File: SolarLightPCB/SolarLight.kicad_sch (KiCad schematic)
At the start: 15 parts, among them J1 I2C, J2 SPI, SW1 Switch, SW2 ON_OFF, U1 TP4056, U2 WeMos_D1_mini

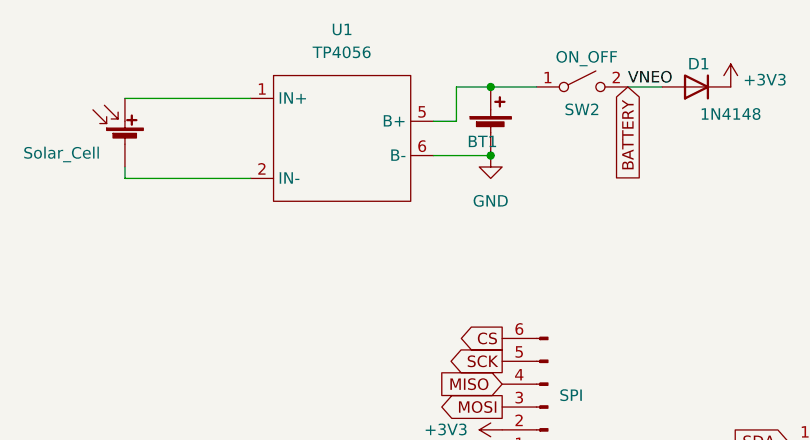
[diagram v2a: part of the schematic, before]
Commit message: Update TP4056 library
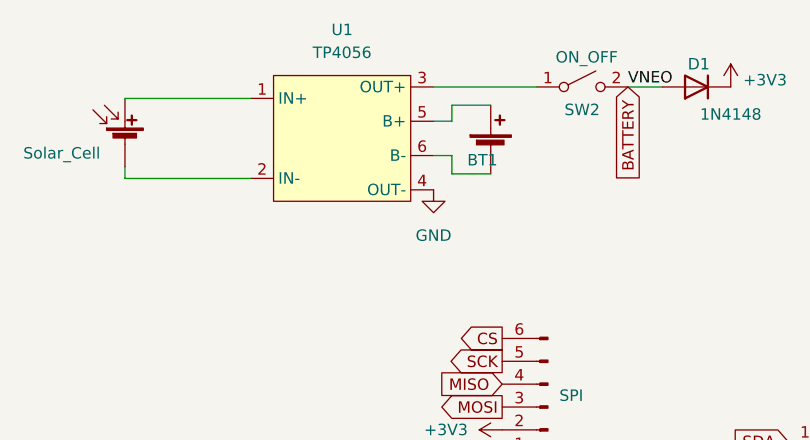
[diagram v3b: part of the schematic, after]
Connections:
- net GND: now also U1.4 (OUT-); no longer BT1.2 (-), U1.6 (B-)
- net at BT1.1 (+), U1.5 (B+): no longer SW2.1 (A)
- new net: BT1.2 (-), U1.6 (B-)
- new net: SW2.1 (A), U1.3 (OUT+)
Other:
- moved on the sheet: BT1
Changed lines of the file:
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@@
     (company "Fablab Zürich / Beat Besmer / Bernd Heistercamp")
   )
-  (junction (at 157.48 38.1) (diameter 0) (color 0 0 0 0)
-  )
   (junction (at 217.932 105.918) (diameter 0) (color 0 0 0 0)
   )
   (junction (at 214.63 97.028) (diameter 0) (color 0 0 0 0)
-  )
-  (junction (at 157.48 45.72) (diameter 0) (color 0 0 0 0)
   )
   (no_connect (at 109.728 103.124))
@@
   (no_connect (at 146.05 114.3))
   (no_connect (at 146.05 116.84))
+  (wire (pts (xy 157.48 40.132) (xy 153.162 40.132))
+    (stroke (width 0) (type default) (color 0 0 0 0))
+  )
+  (wire (pts (xy 153.162 47.752) (xy 157.48 47.752))
+    (stroke (width 0) (type default) (color 0 0 0 0))
+  )
   (wire (pts (xy 214.63 97.028) (xy 221.742 97.028))
     (stroke (width 0) (type default) (color 0 0 0 0))
@@
     (stroke (width 0) (type default) (color 0 0 0 0))
   )
+  (wire (pts (xy 153.162 41.91) (xy 151.13 41.91))
+    (stroke (width 0) (type default) (color 0 0 0 0))
+  )
+  (wire (pts (xy 151.13 45.72) (xy 153.162 45.72))
+    (stroke (width 0) (type default) (color 0 0 0 0))
+  )
   (wire (pts (xy 116.84 48.26) (xy 116.84 46.99))
     (stroke (width 0) (type default) (color 0 0 0 0))
@@
     (stroke (width 0) (type default) (color 0 0 0 0))
   )
-  (wire (pts (xy 153.67 38.1) (xy 153.67 41.91))
-    (stroke (width 0) (type default) (color 0 0 0 0))
-  )
   (wire (pts (xy 130.81 48.26) (xy 116.84 48.26))
     (stroke (width 0) (type default) (color 0 0 0 0))
   )
-  (wire (pts (xy 151.13 41.91) (xy 153.67 41.91))
+  (wire (pts (xy 151.13 38.1) (xy 162.56 38.1))
     (stroke (width 0) (type default) (color 0 0 0 0))
   )
@@
     (stroke (width 0) (type default) (color 0 0 0 0))
   )
-  (wire (pts (xy 151.13 45.72) (xy 157.48 45.72))
-    (stroke (width 0) (type default) (color 0 0 0 0))
-  )
-  (wire (pts (xy 157.48 38.1) (xy 153.67 38.1))
+  (wire (pts (xy 153.162 40.132) (xy 153.162 41.91))
     (stroke (width 0) (type default) (color 0 0 0 0))
   )
@@
     (stroke (width 0) (type default) (color 0 0 0 0))
   )
-  (wire (pts (xy 157.48 38.1) (xy 162.56 38.1))
-    (stroke (width 0) (type default) (color 0 0 0 0))
-  )
   (wire (pts (xy 116.84 39.37) (xy 130.81 39.37))
+    (stroke (width 0) (type default) (color 0 0 0 0))
+  )
+  (wire (pts (xy 153.162 45.72) (xy 153.162 47.752))
     (stroke (width 0) (type default) (color 0 0 0 0))
   )
@@
     (pin "6")
   )
-  (symbol (lib_id "Device:Battery_Cell") (at 157.48 43.18 0) (unit 1)
-    (in_bom yes) (on_board yes)
-    (property "Reference" "BT1" (id 0) (at 158.242 44.196 0)
+  (symbol (lib_id "Device:Battery_Cell") (at 157.48 45.212 0) (unit 1)
+    (in_bom yes) (on_board yes)
+    (property "Reference" "BT1" (id 0) (at 158.242 46.228 0)
       (effects (font (size 1.27 1.27)) (justify right))
     )
-    (property "Value" "Battery_Cell" (id 1) (at 151.765 47.625 0)
-      (effects (font (size 1.27 1.27)) (justify left) hide)
-    )
-    (property "Footprint" "TerminalBlock_Phoenix:TerminalBlock_Phoenix_PT-1,5-2-3.5-H_1x02_P3.50mm_Horizontal" (id 2) (at 157.48 41.656 90)
-      (effects (font (size 1.27 1.27)) hide)
-    )
-    (property "Datasheet" "~" (id 3) (at 157.48 41.656 90)
-      (effects (font (size 1.27 1.27)) hide)
-    )
-    (pin "1")
-    (pin "2")
+    (property "Value" "Battery_Cell" (id 1) (at 151.765 49.657 0)
+      (effects (font (size 1.27 1.27)) (justify left) hide)
+    )
+    (property "Footprint" "TerminalBlock_Phoenix:TerminalBlock_Phoenix_PT-1,5-2-3.5-H_1x02_P3.50mm_Horizontal" (id 2) (at 157.48 43.688 90)
+      (effects (font (size 1.27 1.27)) hide)
+    )
+    (property "Datasheet" "~" (id 3) (at 157.48 43.688 90)
+      (effects (font (size 1.27 1.27)) hide)
+    )
+    (pin "1")
+    (pin "2")
+  )
+  (symbol (lib_id "power:GND") (at 151.13 49.53 0) (unit 1)
+    (in_bom yes) (on_board yes) (fields_autoplaced)
+    (property "Reference" "#PWR0101" (id 0) (at 151.13 55.88 0)
+      (effects (font (size 1.27 1.27)) hide)
+    )
+    (property "Value" "GND" (id 1) (at 151.13 54.61 0))
+    (property "Footprint" "" (id 2) (at 151.13 49.53 0)
+      (effects (font (size 1.27 1.27)) hide)
+    )
+    (property "Datasheet" "" (id 3) (at 151.13 49.53 0)
+      (effects (font (size 1.27 1.27)) hide)
+    )
+    (pin "1")
   )
   (symbol (lib_id "power:GND") (at 217.932 105.918 0) (unit 1)
@@
     (pin "1")
     (pin "2")
+    (pin "3")
+    (pin "4")
     (pin "5")
     (pin "6")
@@
     )
     (property "Datasheet" "" (id 3) (at 109.728 105.664 0)
-      (effects (font (size 1.27 1.27)) hide)
-    )
-    (pin "1")
-  )
-  (symbol (lib_id "power:GND") (at 157.48 45.72 0) (unit 1)
-    (in_bom yes) (on_board yes) (fields_autoplaced)
-    (property "Reference" "#PWR0101" (id 0) (at 157.48 52.07 0)
-      (effects (font (size 1.27 1.27)) hide)
-    )
-    (property "Value" "GND" (id 1) (at 157.48 50.8 0))
-    (property "Footprint" "" (id 2) (at 157.48 45.72 0)
-      (effects (font (size 1.27 1.27)) hide)
-    )
-    (property "Datasheet" "" (id 3) (at 157.48 45.72 0)
       (effects (font (size 1.27 1.27)) hide)
     )
@@
   )
   (symbol_instances
-    (path "/c2806f94-a6b9-42a9-8743-97039d9ba3ce"
+    (path "/246f4d61-f770-43f4-b510-42628efbe170"
       (reference "#PWR0101") (unit 1) (value "GND") (footprint "")
     )

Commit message: Update schematics and bump to version 0.7
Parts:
- added R1: 100k, Resistor_THT:R_Axial_DIN0207_L6.3mm_D2.5mm_P7.62mm_Horizontal, symbol Device:R
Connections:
- net BATTERY: now also BT1.1 (+), U1.5 (B+); no longer D1.2 (A), LIN1.1 (VCC), SW2.2 (B)
- net GND: now also R1.2
- net at BT1.2 (-), U1.6 (B-): now also R1.1
- new net VNEO: D1.2 (A), LIN1.1 (VCC), SW2.2 (B)
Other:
- note added: "Allow measuring the Battery voltage even when the battery is disconnected due to over-discharge"
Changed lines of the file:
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@@
   (title_block
     (title "Solar Light")
-    (date "2022-10-23")
-    (rev "v0.1")
+    (date "2022-12-19")
+    (rev "v0.7")
     (company "Fablab Zürich / Beat Besmer / Bernd Heistercamp")
+  )
+  (junction (at 157.48 47.752) (diameter 0) (color 0 0 0 0)
   )
   (junction (at 217.932 105.918) (diameter 0) (color 0 0 0 0)
@@
     (stroke (width 0) (type default) (color 0 0 0 0))
   )
+  (text "Allow measuring the Battery voltage \neven when the battery is disconnected \ndue to over-discharge"
+    (at 164.338 54.864 0)
+    (effects (font (size 1.27 1.27)) (justify left bottom))
+  )
   (label "VNEO" (at 172.72 38.1 0)
     (effects (font (size 1.27 1.27)) (justify left bottom))
@@
     )
   )
-  (global_label "BATTERY" (shape input) (at 172.72 38.1 270) (fields_autoplaced)
-    (effects (font (size 1.27 1.27)) (justify right))
-    (property "Intersheet References" "${INTERSHEET_REFS}" (id 0) (at 172.7994 48.3145 90)
-      (effects (font (size 1.27 1.27)) (justify right) hide)
+  (global_label "BATTERY" (shape input) (at 155.194 40.132 90) (fields_autoplaced)
+    (effects (font (size 1.27 1.27)) (justify left))
+    (property "Intersheet References" "${INTERSHEET_REFS}" (id 0) (at 155.1146 29.9175 90)
+      (effects (font (size 1.27 1.27)) (justify left) hide)
     )
   )
@@
     )
     (pin "1")
+  )
+  (symbol (lib_id "Device:R") (at 157.48 51.562 0) (unit 1)
+    (in_bom yes) (on_board yes) (fields_autoplaced)
+    (property "Reference" "R1" (id 0) (at 159.258 50.2919 0)
+      (effects (font (size 1.27 1.27)) (justify left))
+    )
+    (property "Value" "100k" (id 1) (at 159.258 52.8319 0)
+      (effects (font (size 1.27 1.27)) (justify left))
+    )
+    (property "Footprint" "Resistor_THT:R_Axial_DIN0207_L6.3mm_D2.5mm_P7.62mm_Horizontal" (id 2) (at 155.702 51.562 90)
+      (effects (font (size 1.27 1.27)) hide)
+    )
+    (property "Datasheet" "~" (id 3) (at 157.48 51.562 0)
+      (effects (font (size 1.27 1.27)) hide)
+    )
+    (pin "1")
+    (pin "2")
   )
   (symbol (lib_id "power:GND") (at 210.058 44.958 0) (unit 1)
@@
     (pin "3")
   )
+  (symbol (lib_id "power:GND") (at 157.48 55.372 0) (unit 1)
+    (in_bom yes) (on_board yes) (fields_autoplaced)
+    (property "Reference" "#PWR0102" (id 0) (at 157.48 61.722 0)
+      (effects (font (size 1.27 1.27)) hide)
+    )
+    (property "Value" "GND" (id 1) (at 157.48 60.452 0))
+    (property "Footprint" "" (id 2) (at 157.48 55.372 0)
+      (effects (font (size 1.27 1.27)) hide)
+    )
+    (property "Datasheet" "" (id 3) (at 157.48 55.372 0)
+      (effects (font (size 1.27 1.27)) hide)
+    )
+    (pin "1")
+  )
   (symbol (lib_id "Device:C_Polarized") (at 210.058 41.148 0) (unit 1)
     (in_bom yes) (on_board yes)
@@
       (reference "#PWR0101") (unit 1) (value "GND") (footprint "")
     )
+    (path "/e2ff7594-20a7-4214-af88-d4c574e2691c"
+      (reference "#PWR0102") (unit 1) (value "GND") (footprint "")
+    )
     (path "/4994b6ae-8df2-4c30-941b-b6aef74040b1"
       (reference "#PWR0103") (unit 1) (value "GND") (footprint "")
@@
       (reference "LOUT1") (unit 1) (value "LEDs_Out") (footprint "NeopixelStrip:LED-Strip")
     )
+    (path "/34b8c0fa-795e-4e33-924b-c6ecc1885144"
+      (reference "R1") (unit 1) (value "100k") (footprint "Resistor_THT:R_Axial_DIN0207_L6.3mm_D2.5mm_P7.62mm_Horizontal")
+    )
     (path "/d85e1e13-e38e-4950-90e0-28ee56a30aec"

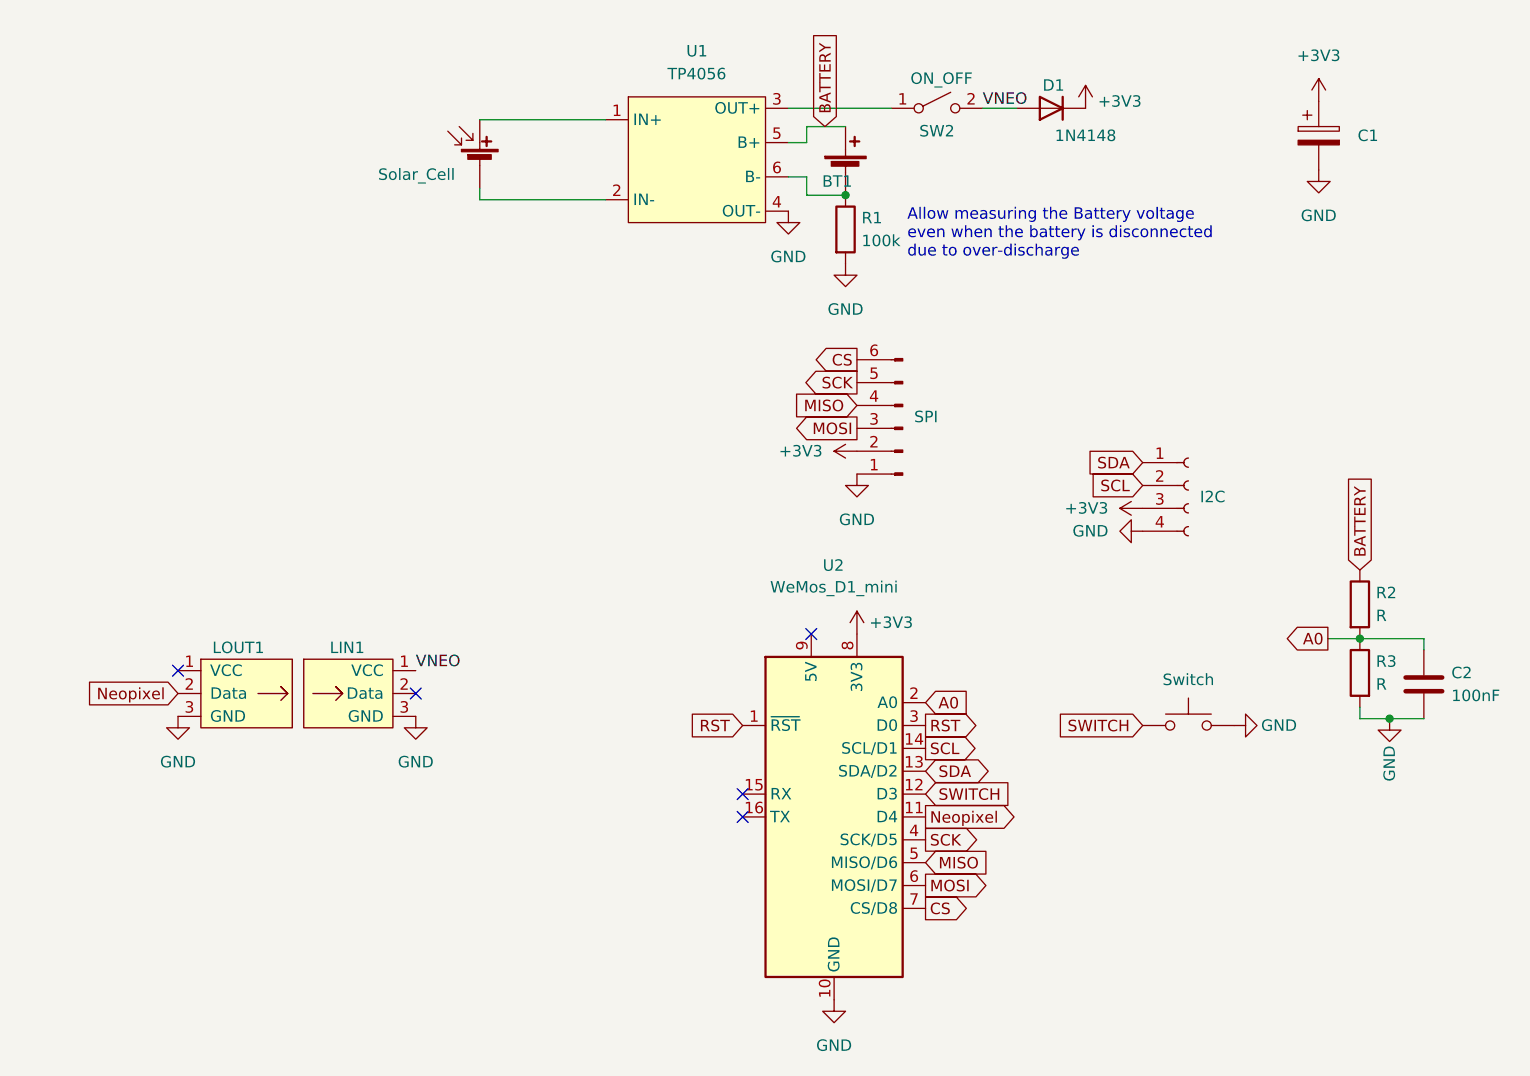
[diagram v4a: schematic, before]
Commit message: Use the 5V to 3V3 regulator of the Wemos D1
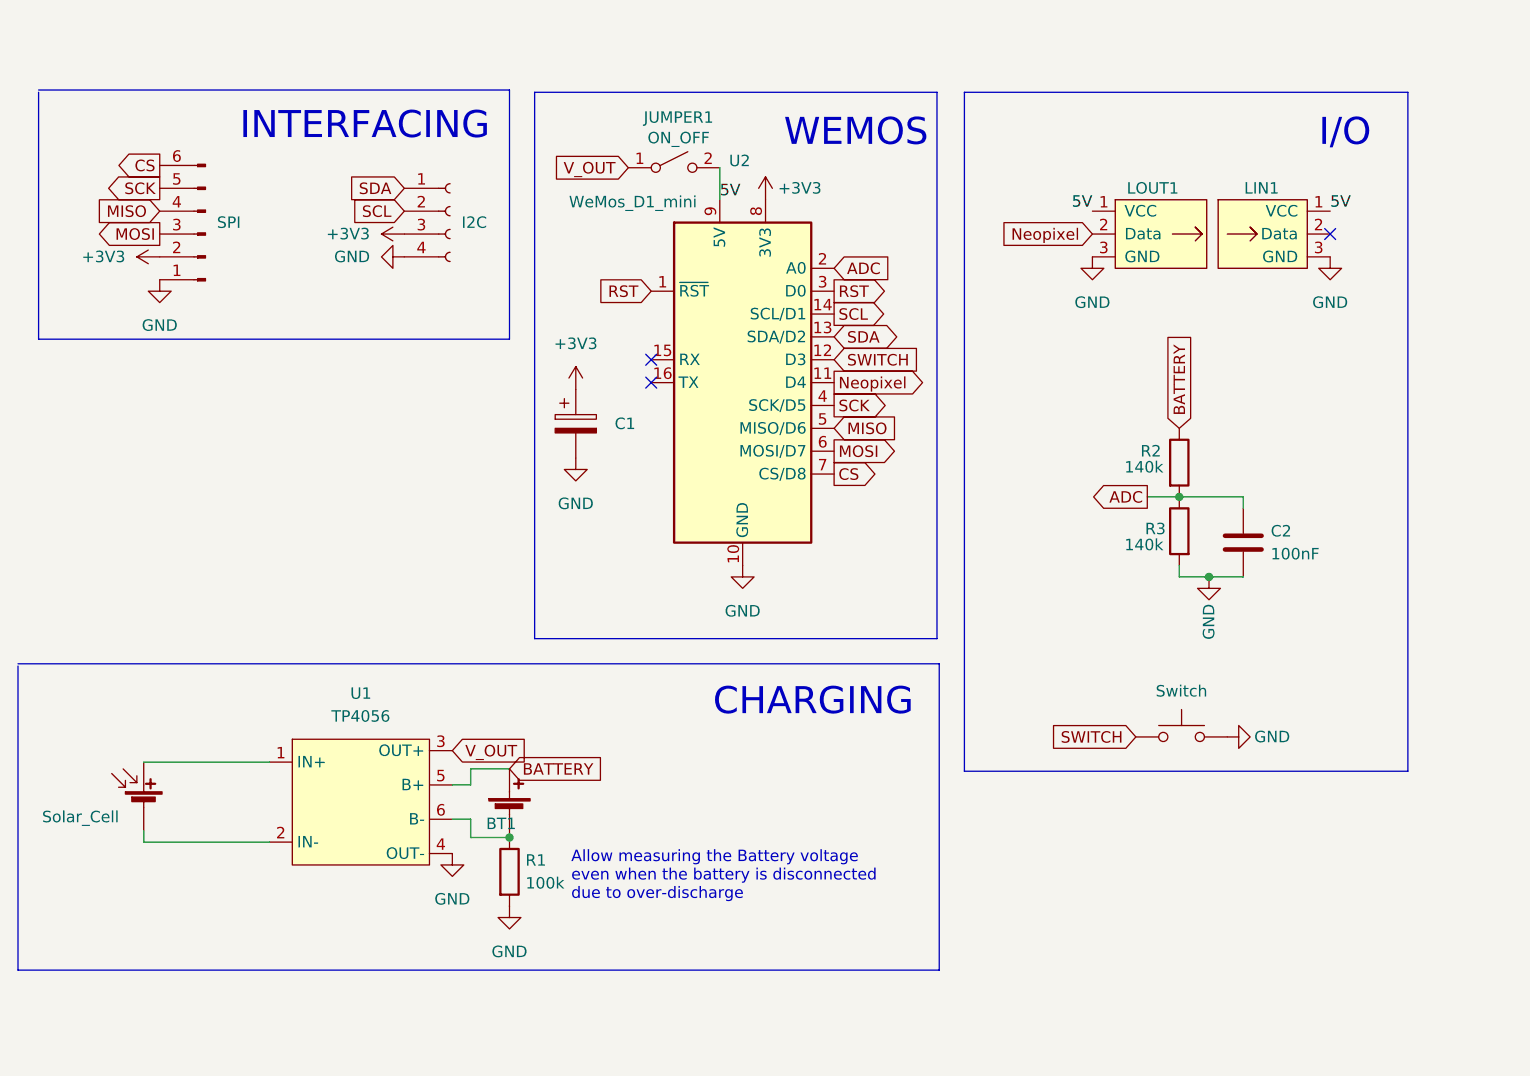
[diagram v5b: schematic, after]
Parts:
- removed D1: 1N4148, Diode_THT:D_DO-35_SOD27_P7.62mm_Horizontal, symbol Diode:1N4148
- removed SW2: ON_OFF, Connector_PinHeader_2.54mm:PinHeader_1x03_P2.54mm_Vertical, symbol Switch:SW_SPST
- added JUMPER1: ON_OFF, Connector_PinHeader_2.54mm:PinHeader_1x03_P2.54mm_Vertical, symbol Switch:SW_SPST
- R2, R3: value R -> 140k
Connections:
- net VNEO is gone; now on net 5V: LIN1.1 (VCC)
- net V_OUT: now reaches U1.3 (OUT+)
- net V_OUT: now also JUMPER1.1 (A)
- net 5V: now reaches U2.9 (5V)
- net 5V: now also LOUT1.1 (VCC), JUMPER1.2 (B)
- net A0 renamed ADC
- no-connect marks 5 -> 3
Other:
- note added: "CHARGING"
- note added: "I/O"
- note added: "INTERFACING"
- note added: "WEMOS"
- moved on the sheet: BT1, C1, C2, LIN1, LOUT1, R1, R2, R3, U1, U2

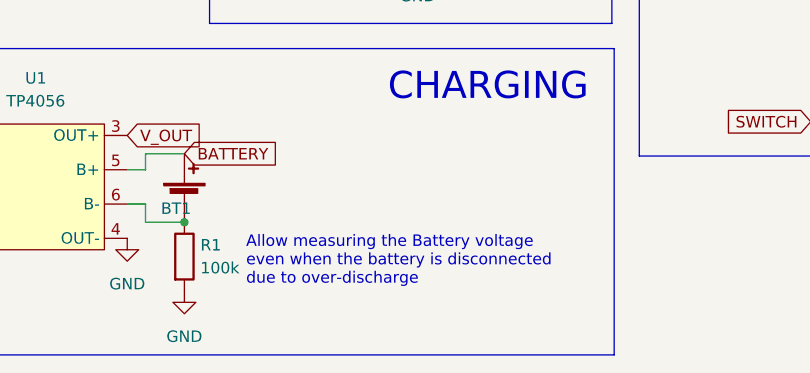
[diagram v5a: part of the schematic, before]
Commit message: Remove the resistor for measuring the battery voltage even in the disconnected state
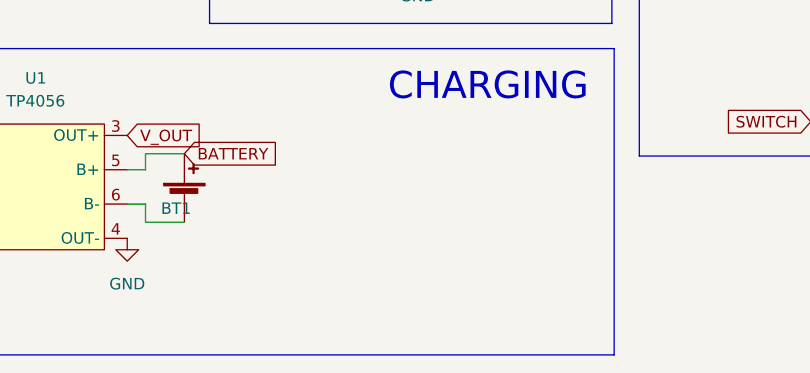
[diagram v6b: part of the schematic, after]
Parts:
- removed R1: 100k, Resistor_THT:R_Axial_DIN0207_L6.3mm_D2.5mm_P7.62mm_Horizontal, symbol Device:R
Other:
- note removed: "Allow measuring the Battery voltage even when the battery is disconnected due to over-discharge"
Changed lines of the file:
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@@
     (company "Fablab Zürich / Beat Besmer / Bernd Heistercamp")
-  )
-  (junction (at 120.142 119.126) (diameter 0) (color 0 0 0 0)
   )
   (junction (at 197.866 90.17) (diameter 0) (color 0 0 0 0)
@@
     (effects (font (size 3 3)) (justify left bottom))
   )
-  (text "Allow measuring the Battery voltage \neven when the battery is disconnected \ndue to over-discharge"
-    (at 127 126.238 0)
-    (effects (font (size 1.27 1.27)) (justify left bottom))
-  )
   (text "I/O" (at 210.058 42.672 0)
     (effects (font (size 3 3)) (justify left bottom))
@@
     )
     (pin "1")
-  )
-  (symbol (lib_id "Device:R") (at 120.142 122.936 0) (unit 1)
-    (in_bom yes) (on_board yes) (fields_autoplaced)
-    (property "Reference" "R1" (id 0) (at 121.92 121.6659 0)
-      (effects (font (size 1.27 1.27)) (justify left))
-    )
-    (property "Value" "100k" (id 1) (at 121.92 124.2059 0)
-      (effects (font (size 1.27 1.27)) (justify left))
-    )
-    (property "Footprint" "Resistor_THT:R_Axial_DIN0207_L6.3mm_D2.5mm_P7.62mm_Horizontal" (id 2) (at 118.364 122.936 90)
-      (effects (font (size 1.27 1.27)) hide)
-    )
-    (property "Datasheet" "~" (id 3) (at 120.142 122.936 0)
-      (effects (font (size 1.27 1.27)) hide)
-    )
-    (pin "1")
-    (pin "2")
   )
   (symbol (lib_id "power:GND") (at 127.508 76.962 0) (unit 1)
@@
     (pin "3")
   )
-  (symbol (lib_id "power:GND") (at 120.142 126.746 0) (unit 1)
-    (in_bom yes) (on_board yes) (fields_autoplaced)
-    (property "Reference" "#PWR0102" (id 0) (at 120.142 133.096 0)
-      (effects (font (size 1.27 1.27)) hide)
-    )
-    (property "Value" "GND" (id 1) (at 120.142 131.826 0))
-    (property "Footprint" "" (id 2) (at 120.142 126.746 0)
-      (effects (font (size 1.27 1.27)) hide)
-    )
-    (property "Datasheet" "" (id 3) (at 120.142 126.746 0)
-      (effects (font (size 1.27 1.27)) hide)
-    )
-    (pin "1")
-  )
   (symbol (lib_id "Device:C_Polarized") (at 127.508 73.152 0) (unit 1)
     (in_bom yes) (on_board yes)
@@
       (reference "#PWR0101") (unit 1) (value "GND") (footprint "")
     )
-    (path "/e2ff7594-20a7-4214-af88-d4c574e2691c"
-      (reference "#PWR0102") (unit 1) (value "GND") (footprint "")
-    )
     (path "/4994b6ae-8df2-4c30-941b-b6aef74040b1"
       (reference "#PWR0103") (unit 1) (value "GND") (footprint "")
@@
       (reference "LOUT1") (unit 1) (value "LEDs_Out") (footprint "NeopixelStrip:LED-Strip")
     )
-    (path "/34b8c0fa-795e-4e33-924b-c6ecc1885144"
-      (reference "R1") (unit 1) (value "100k") (footprint "Resistor_THT:R_Axial_DIN0207_L6.3mm_D2.5mm_P7.62mm_Horizontal")
-    )
     (path "/d85e1e13-e38e-4950-90e0-28ee56a30aec"
